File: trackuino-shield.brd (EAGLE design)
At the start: 67.3 x 53.3 mm, 19 parts, among them IC2 AP1117, M2 HX1, Q1 IRLD110, U1 LM60 int, X1 BU-SMA-V, X2 Vin, X3 LM60 ext, X4 Buzzer

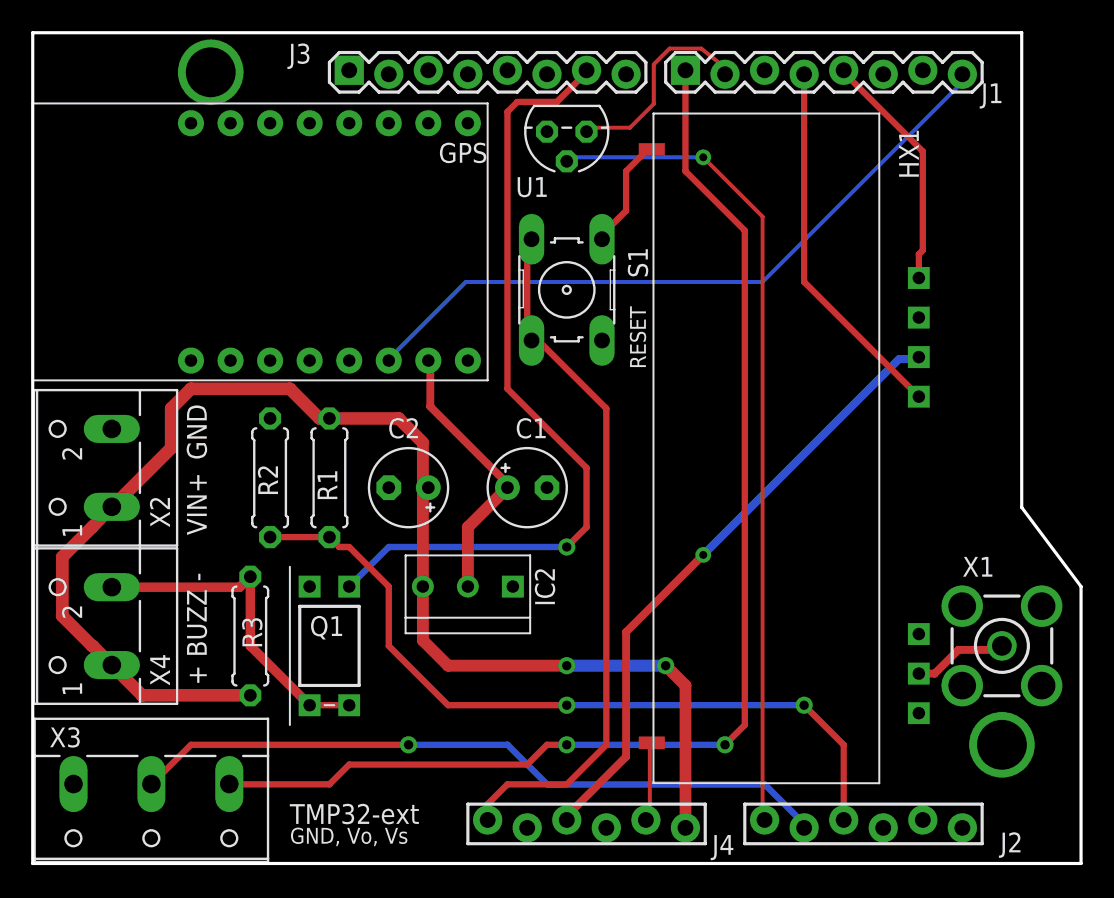
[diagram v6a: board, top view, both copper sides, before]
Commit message: Fixed sheaff's comments and separated the ground plane from the radiometrix
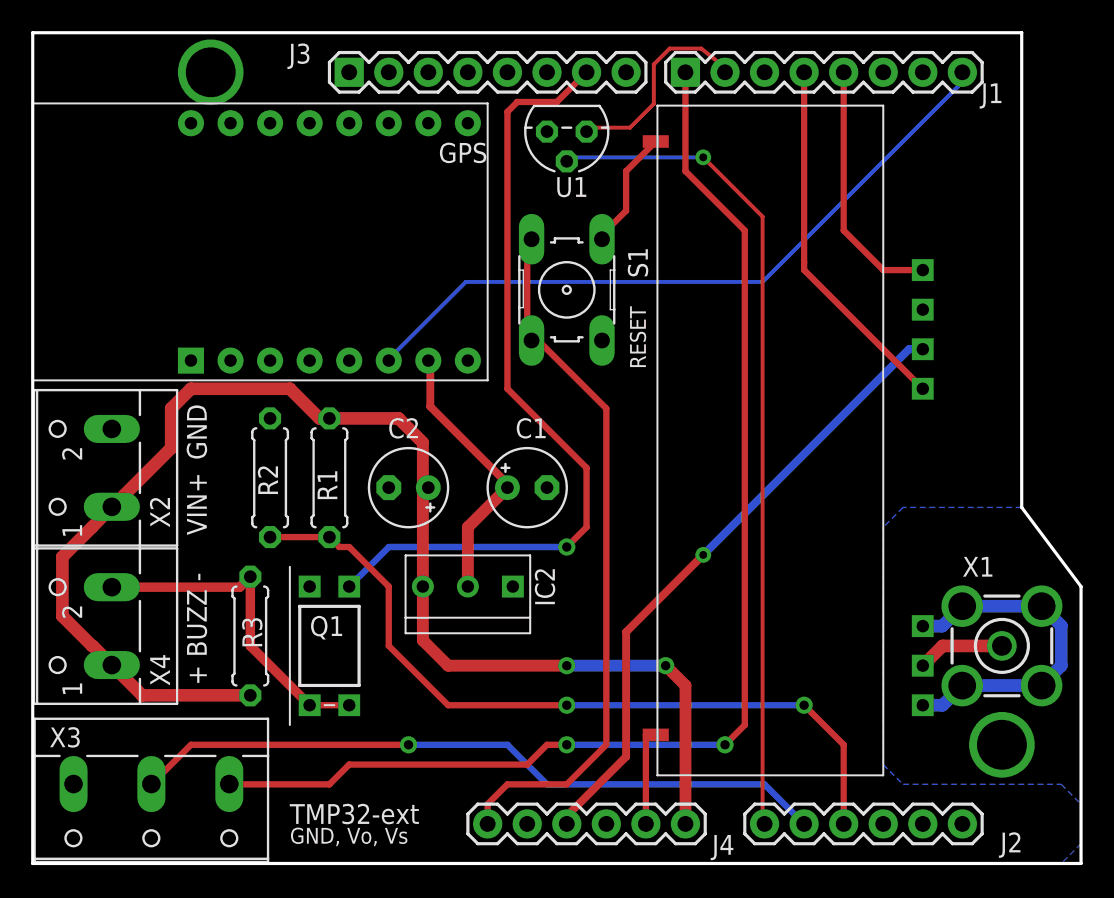
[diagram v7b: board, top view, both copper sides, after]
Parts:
- removed M2: HX1, trackuino:HX1
- added M1: HX1, trackuino:HX1
- J1, J3: device SparkFun:1X08_LOCK -> SparkFun-Connectors:1X08
- J2, J4: device SparkFun:1X06_FEMALE_LOCK.010 -> SparkFun-Connectors:1X06
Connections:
- removed net RFOUT: M2.RFOUT, X1.1
- new net N$2: M1.RFOUT, X1.1
- new net RFGND: M1.RFGND1, M1.RFGND2, X1.2, X1.3, X1.4, X1.5
- net +5V: now also M1.VCC; no longer M2.VCC
- net D3: now also M1.TXD; no longer M2.TXD
- net D4: now also M1.EN; no longer M2.EN
- net GND: now also M1.0V, M1.BODYGND1, M1.BODYGND2; no longer M2.0V, M2.BODYGND1, M2.BODYGND2, M2.RFGND1, M2.RFGND2, X1.2, X1.3, X1.4, X1.5
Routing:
- net RFGND: track 0.00 -> 22.5 mm
- net RFOUT: track 6.12 -> 0.00 mm
- net N$2: track 0.00 -> 5.61 mm
- net GND: track 12.4 -> 14.1 mm
- net D3: track 15.5 -> 16.3 mm
- net +5V: track 39.8 -> 40.5 mm

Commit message: Added logo
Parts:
- added U$1: (no value), tr:FLAGS_SM
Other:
- board text added: "Trackuino THT 2.2+"
- board text removed: "Trackuino Shield 2.2"
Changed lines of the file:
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@@
 <setting verticaltext="up"/>
 </settings>
-<grid distance="50" unitdist="mil" unit="mil" style="lines" multiple="1" display="yes" altdistance="25" altunitdist="mil" altunit="mil"/>
+<grid distance="0.025" unitdist="inch" unit="inch" style="lines" multiple="1" display="yes" altdistance="0.0125" altunitdist="inch" altunit="inch"/>
 <layers>
-<layer number="1" name="Top" color="4" fill="1" visible="yes" active="yes"/>
+<layer number="1" name="Top" color="4" fill="1" visible="no" active="yes"/>
 <layer number="2" name="Route2" color="1" fill="3" visible="no" active="yes"/>
 <layer number="3" name="Route3" color="4" fill="3" visible="no" active="yes"/>
@@
 <layer number="17" name="Pads" color="2" fill="1" visible="yes" active="yes"/>
 <layer number="18" name="Vias" color="2" fill="1" visible="yes" active="yes"/>
-<layer number="19" name="Unrouted" color="6" fill="1" visible="yes" active="yes"/>
+<layer number="19" name="Unrouted" color="6" fill="1" visible="no" active="yes"/>
 <layer number="20" name="Dimension" color="14" fill="1" visible="yes" active="yes"/>
-<layer number="21" name="tPlace" color="16" fill="1" visible="yes" active="yes"/>
+<layer number="21" name="tPlace" color="16" fill="1" visible="no" active="yes"/>
 <layer number="22" name="bPlace" color="14" fill="1" visible="yes" active="yes"/>
-<layer number="23" name="tOrigins" color="15" fill="1" visible="yes" active="yes"/>
+<layer number="23" name="tOrigins" color="15" fill="1" visible="no" active="yes"/>
 <layer number="24" name="bOrigins" color="15" fill="1" visible="yes" active="yes"/>
 <layer number="25" name="tNames" color="7" fill="1" visible="no" active="yes"/>
-<layer number="26" name="bNames" color="7" fill="1" visible="no" active="yes"/>
+<layer number="26" name="bNames" color="7" fill="1" visible="yes" active="yes"/>
 <layer number="27" name="tValues" color="7" fill="1" visible="no" active="yes"/>
 <layer number="28" name="bValues" color="7" fill="1" visible="no" active="yes"/>
@@
 <layer number="42" name="bRestrict" color="1" fill="10" visible="no" active="yes"/>
 <layer number="43" name="vRestrict" color="2" fill="10" visible="no" active="yes"/>
-<layer number="44" name="Drills" color="7" fill="1" visible="no" active="yes"/>
+<layer number="44" name="Drills" color="7" fill="1" visible="yes" active="yes"/>
 <layer number="45" name="Holes" color="7" fill="1" visible="yes" active="yes"/>
 <layer number="46" name="Milling" color="3" fill="1" visible="no" active="yes"/>
@@
 <layer number="49" name="Reference" color="7" fill="1" visible="no" active="yes"/>
 <layer number="50" name="dxf" color="7" fill="1" visible="no" active="yes"/>
-<layer number="51" name="tDocu" color="6" fill="1" visible="yes" active="yes"/>
+<layer number="51" name="tDocu" color="6" fill="1" visible="no" active="yes"/>
 <layer number="52" name="bDocu" color="7" fill="1" visible="no" active="yes"/>
 <layer number="53" name="tGND_GNDA" color="7" fill="9" visible="no" active="no"/>
@@
 <text x="11.176" y="21.082" size="1.27" layer="25" font="vector" rot="R90">VIN+</text>
 <text x="39.37" y="31.75" size="1.016" layer="25" font="vector" rot="R90">RESET</text>
-<text x="52.07" y="6.35" size="2.54" layer="48" font="vector" rot="MR90">Trackuino Shield 2.2</text>
+<text x="52.07" y="6.35" size="2.54" layer="26" font="vector" rot="MR90">Trackuino THT 2.2+</text>
 <text x="49.53" y="6.35" size="1.27" layer="48" font="vector" rot="MR90">http://trackuino.org</text>
 <text x="11.176" y="25.908" size="1.27" layer="25" rot="R90">GND</text>
@@
 <text x="45.72" y="6.35" size="1.27" layer="48" font="vector" rot="MR90">5V: bridge J6, J8; buffer on IC4</text>
 <text x="43.18" y="6.35" size="1.27" layer="48" font="vector" rot="MR90">3.3V: bridge J7; buffers on IC3, IC5</text>
-<rectangle x1="21.59" y1="8.89" x2="34.29" y2="19.05" layer="30"/>
-<rectangle x1="21.59" y1="8.89" x2="34.29" y2="19.05" layer="29"/>
+<rectangle x1="1.27" y1="35.56" x2="24.13" y2="45.72" layer="26"/>
 </plain>
 <attributes>
@@
 </class>
 </classes>
-<designrules name="SparkFun">
-<description language="en">&lt;b&gt;SparkFun EAGLE Design Rules&lt;/b&gt;
+<designrules name="LaenPCBOrder">
+<description language="de">&lt;b&gt;EAGLE Design Rules&lt;/b&gt;
 &lt;p&gt;
-The default Design Rules have been set to cover
-a wide range of applications. Your particular design
-may have different requirements, so please make the
-necessary adjustments and save your customized
-design rules under a new name.</description>
+Die Standard-Design-Rules sind so gewählt, dass sie für
+die meisten Anwendungen passen. Sollte ihre Platine
+besondere Anforderungen haben, treffen Sie die erforderlichen
+Einstellungen hier und speichern die Design Rules unter
+einem neuen Namen ab.</description>
+<description language="en">&lt;b&gt;Laen's PCB Order Design Rules&lt;/b&gt;
+&lt;p&gt;
+Please make sure your boards conform to these design rules.</description>
 <param name="layerSetup" value="(1*16)"/>
-<param name="mtCopper" value="0.035mm 0.035mm 0.035mm 0.035mm 0.035mm 0.035mm 0.035mm 0.035mm 0.035mm 0.035mm 0.035mm 0.035mm 0.035mm 0.035mm 0.035mm 0.035mm"/>
-<param name="mtIsolate" value="1.5mm 0.15mm 0.2mm 0.15mm 0.2mm 0.15mm 0.2mm 0.15mm 0.2mm 0.15mm 0.2mm 0.15mm 0.2mm 0.15mm 0.2mm"/>
-<param name="mdWireWire" value="8mil"/>
-<param name="mdWirePad" value="8mil"/>
-<param name="mdWireVia" value="8mil"/>
-<param name="mdPadPad" value="8mil"/>
-<param name="mdPadVia" value="8mil"/>
-<param name="mdViaVia" value="8mil"/>
-<param name="mdSmdPad" value="8mil"/>
-<param name="mdSmdVia" value="8mil"/>
-<param name="mdSmdSmd" value="8mil"/>
+<param name="mtCopper" value="0.0356mm 0.0356mm 0.0356mm 0.0356mm 0.0356mm 0.0356mm 0.0356mm 0.0356mm 0.0356mm 0.0356mm 0.0356mm 0.0356mm 0.0356mm 0.0356mm 0.0356mm 0.0356mm"/>
+<param name="mtIsolate" value="1.5011mm 0.1499mm 0.2007mm 0.1499mm 0.2007mm 0.1499mm 0.2007mm 0.1499mm 0.2007mm 0.1499mm 0.2007mm 0.1499mm 0.2007mm 0.1499mm 0.2007mm"/>
+<param name="mdWireWire" value="6mil"/>
+<param name="mdWirePad" value="6mil"/>
+<param name="mdWireVia" value="6mil"/>
+<param name="mdPadPad" value="6mil"/>
+<param name="mdPadVia" value="6mil"/>
+<param name="mdViaVia" value="6mil"/>
+<param name="mdSmdPad" value="6mil"/>
+<param name="mdSmdVia" value="6mil"/>
+<param name="mdSmdSmd" value="6mil"/>
 <param name="mdViaViaSameLayer" value="8mil"/>
 <param name="mnLayersViaInSmd" value="2"/>
-<param name="mdCopperDimension" value="10mil"/>
-<param name="mdDrill" value="8mil"/>
+<param name="mdCopperDimension" value="15mil"/>
+<param name="mdDrill" value="6mil"/>
 <param name="mdSmdStop" value="0mil"/>
-<param name="msWidth" value="8mil"/>
-<param name="msDrill" value="20mil"/>
-<param name="msMicroVia" value="9.99mm"/>
+<param name="msWidth" value="6mil"/>
+<param name="msDrill" value="13mil"/>
+<param name="msMicroVia" value="13mil"/>
 <param name="msBlindViaRatio" value="0.5"/>
 <param name="rvPadTop" value="0.25"/>
@@
 <param name="rvMicroViaOuter" value="0.25"/>
 <param name="rvMicroViaInner" value="0.25"/>
-<param name="rlMinPadTop" value="12mil"/>
+<param name="rlMinPadTop" value="7mil"/>
 <param name="rlMaxPadTop" value="20mil"/>
-<param name="rlMinPadInner" value="10mil"/>
+<param name="rlMinPadInner" value="7mil"/>
 <param name="rlMaxPadInner" value="20mil"/>
-<param name="rlMinPadBottom" value="12mil"/>
+<param name="rlMinPadBottom" value="7mil"/>
 <param name="rlMaxPadBottom" value="20mil"/>
-<param name="rlMinViaOuter" value="10mil"/>
+<param name="rlMinViaOuter" value="7mil"/>
 <param name="rlMaxViaOuter" value="20mil"/>
-<param name="rlMinViaInner" value="10mil"/>
+<param name="rlMinViaInner" value="7mil"/>
 <param name="rlMaxViaInner" value="20mil"/>
 <param name="rlMinMicroViaOuter" value="4mil"/>
@@
 <param name="mvStopFrame" value="1"/>
 <param name="mvCreamFrame" value="0"/>
-<param name="mlMinStopFrame" value="4mil"/>
-<param name="mlMaxStopFrame" value="4mil"/>
+<param name="mlMinStopFrame" value="3mil"/>
+<param name="mlMaxStopFrame" value="3mil"/>
 <param name="mlMinCreamFrame" value="0mil"/>
 <param name="mlMaxCreamFrame" value="0mil"/>
-<param name="mlViaStopLimit" value="25mil"/>
+<param name="mlViaStopLimit" value="0mil"/>
 <param name="srRoundness" value="0"/>
 <param name="srMinRoundness" value="0mil"/>
@@
 <attribute name="VALUE" x="17.78" y="12.7" size="0.508" layer="27" font="vector"/>
 </element>
-<element name="M1" library="trackuino" package="HX1" value="HX1" x="48.26" y="10.16" rot="R90"/>
+<element name="M1" library="trackuino" package="HX1" value="HX1" x="48.26" y="10.16" smashed="yes" rot="R90">
+<attribute name="NAME" x="57.15" y="44.45" size="1.27" layer="25" font="vector" rot="R90"/>
+<attribute name="VALUE" x="57.15" y="20.32" size="1.27" layer="25" font="vector" rot="R90"/>
+</element>
 <element name="X1" library="con-coax" package="BU-SMA-V" value="BU-SMA-V" x="62.23" y="13.97">
 <attribute name="OC_NEWARK" value="unknown" x="62.23" y="13.97" size="1.778" layer="27" font="vector" ratio="15" display="off"/>
@@
 <attribute name="OC_FARNELL" value="unknown" x="62.23" y="13.97" size="1.778" layer="27" font="vector" ratio="15" display="off"/>
 </element>
+<element name="U$1" library="tr" package="FLAGS_SM" value="" x="41.275" y="27.94"/>
 </elements>
 <signals>
